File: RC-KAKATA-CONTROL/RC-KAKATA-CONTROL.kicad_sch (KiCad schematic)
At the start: 67 parts, among them J1 Conn_02x20_Socket_DG250T-5.0-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, J10 DB125-2.54-4P-GN, J12 Conn_01x07, J25 Conn_02x20_Socket_DG250T-5.0-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, J6 Raspberry_Pi_2x20_PTH, J8 DB125-2.54-4P-GN, U3 STM32H743IIT6, U8 W25Q128JVSIQTR, X1 SMD3225-4, X2 Q13MC3061000300

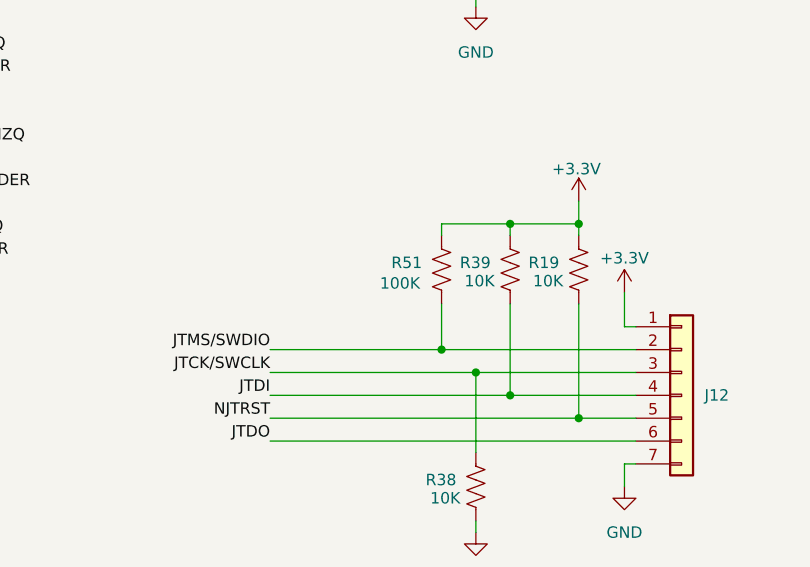
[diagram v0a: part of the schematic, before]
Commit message: Asignacion Ref. LCSC BOM
Asignacion de número de piezas de LCSC.
Queda pendiente cristal 25MHz y Power Supply.
Att.: Juan y Eric
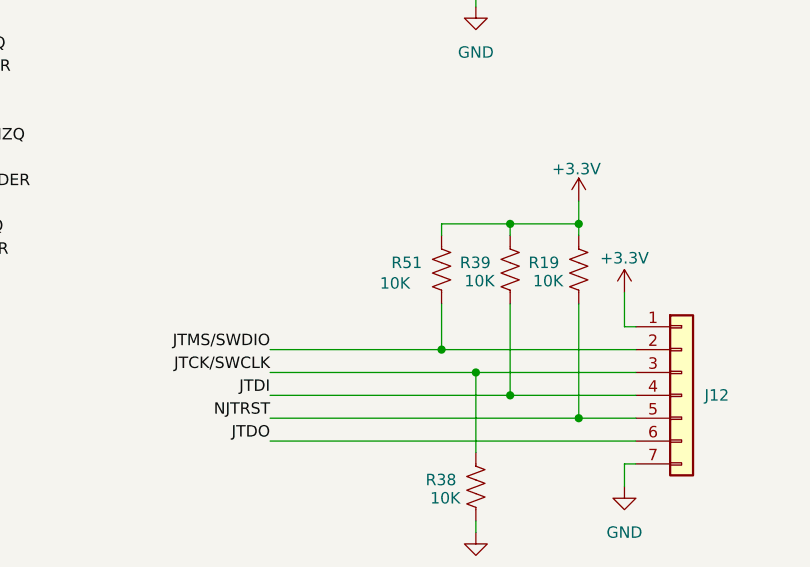
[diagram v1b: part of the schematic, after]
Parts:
- C19, C24, C29, C30, C31, C32, C51, C52, C53, C54: LCSC Part (none) -> C109474
- C36, C37: LCSC Part (none) -> C519117
- C38, C39: LCSC Part (none) -> C1850490
- C50: LCSC Part (none) -> C106248
- J1, J25, J6: now left out of the parts list
- J12: LCSC Part (none) -> C5360900
- LED5: LCSC Part (none) -> C19171390
- R1, R16, R17, R19, R2, R3, R38, R39, R4, R45: LCSC Part (none) -> C95204
- R18: LCSC Part (none) -> C705763
- R20, R21, R22, R23, R24, R25, R26, R27, R28, R29, R30, R31, R32, R33, R34, R35, R36, R37: LCSC Part (none) -> C114065
- R46, R47, R48, R49, R50: LCSC Part (none) -> C108661
- R51: value 100K -> 10K; LCSC Part (none) -> C95204
